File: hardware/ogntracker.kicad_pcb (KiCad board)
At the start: 2 copper layers, 50 x 84 mm, 14 parts, among them J1 ANT, J2 CONN_PWR, U1 STM32DEVBOARD, U2 RFM69HW, U3 VK2828U7G5LF

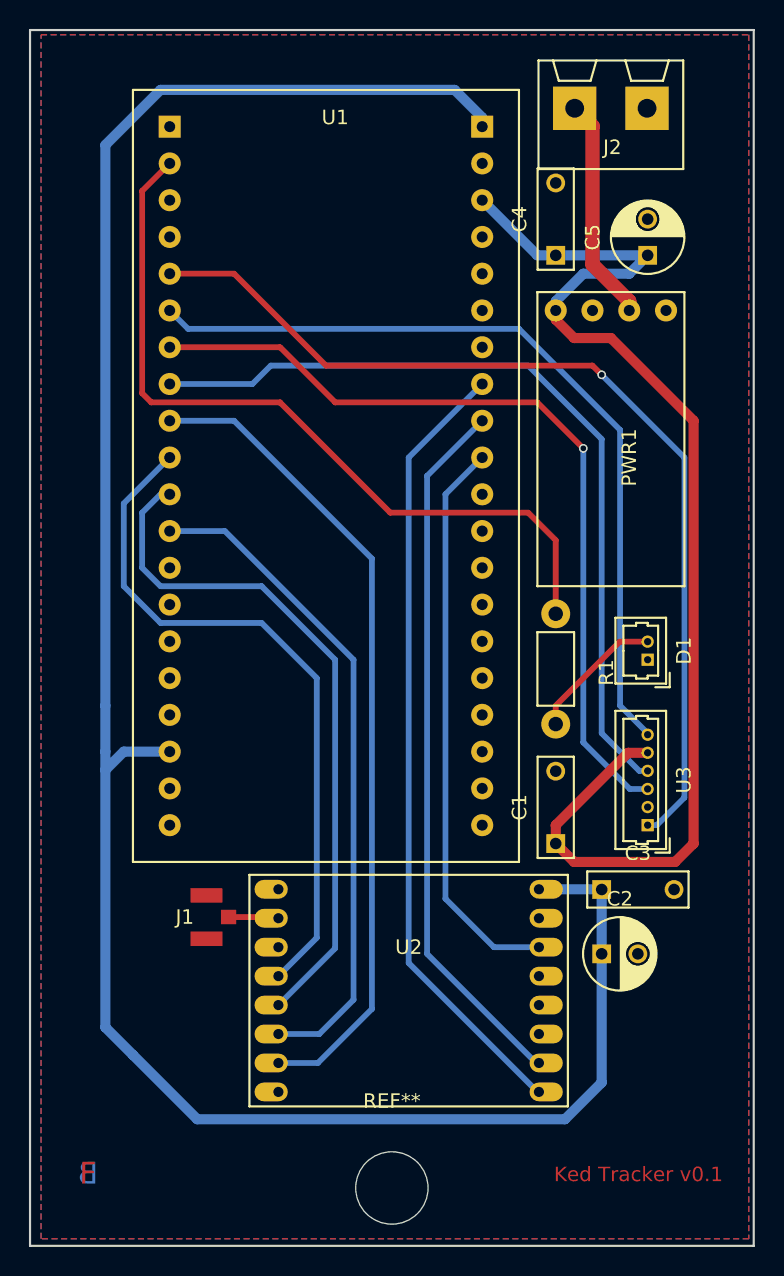
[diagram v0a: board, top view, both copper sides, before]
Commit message: Improvements to make hand-made board easier to produce
 * Wider copper base for pins
 * Proper size of CPU board
 * Added console headers
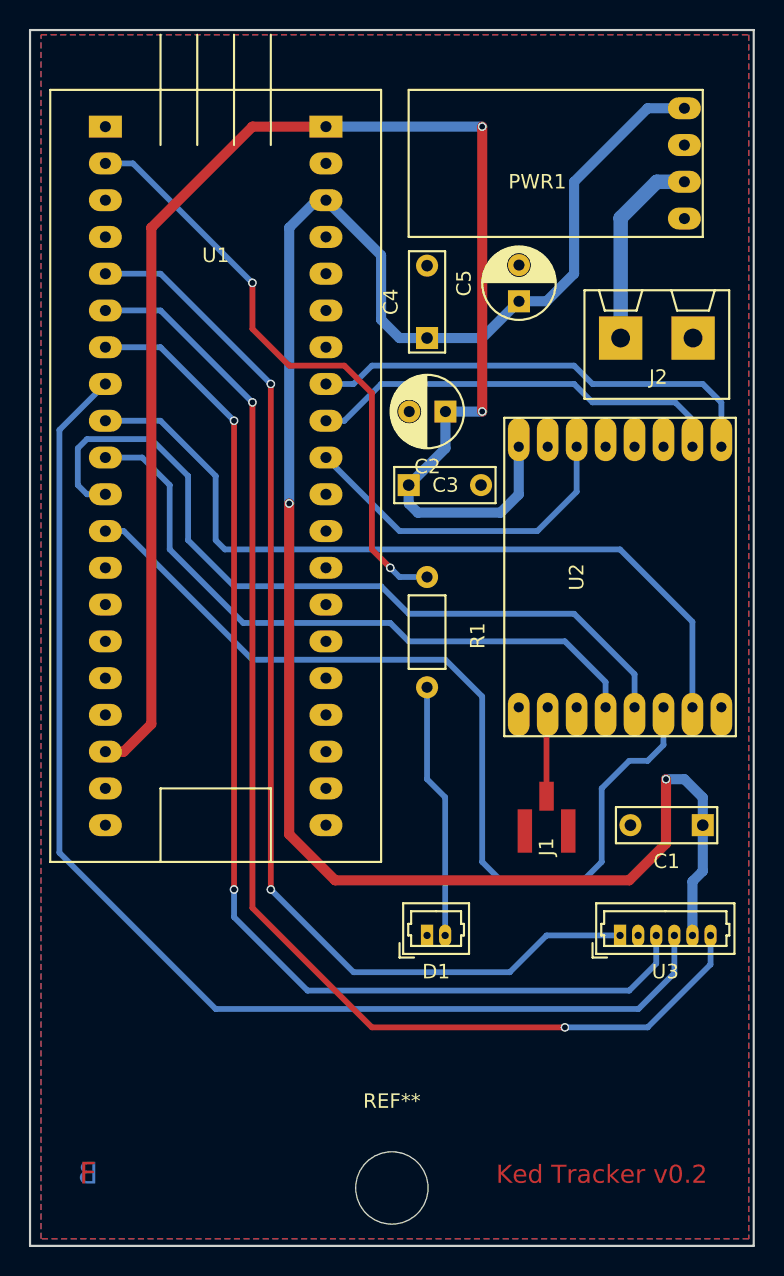
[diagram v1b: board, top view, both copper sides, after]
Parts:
- C1, C3, C4: footprint Capacitors_ThroughHole:C_Rect_L7_W2.5_P5 -> OGN Tracker:C_Rect_L7_W2.5_P5
- C2, C5: footprint Capacitors_ThroughHole:C_Radial_D5_L11_P2.5 -> OGN Tracker:C_Radial_D5_L11_P2.5
- D1: footprint Connectors_Molex:Molex_PicoBlade_53047-0210_02x1.25mm_Straight -> OGN Tracker:Molex_PicoBlade_53047-0210_02x1.25mm_Straight
- J2: footprint Kedder Terminals:XY301-5-2 -> OGN Tracker:XY301-5-2
- R1: footprint Resistors_ThroughHole:Resistor_Horizontal_RM7mm -> OGN Tracker:Resistor_Horizontal_RM7mm
- U3: footprint Connectors_Molex:Molex_PicoBlade_53047-0610_06x1.25mm_Straight -> OGN Tracker:Molex_PicoBlade_53047-0610_06x1.25mm_Straight
- moved C2 39.0 mm to (159.4, 99.1), turned to 180 degrees
- moved U2 32.1 mm to (171.4, 110.5), turned to 270 degrees
- moved C3 31.0 mm to (156.8, 104.1)
- moved D1 24.4 mm to (158.1, 135.3), turned to 0 degrees
- moved J1 24.3 mm to (166.4, 127.6), turned to 90 degrees
- moved J2 16.2 mm to (174.0, 94.0)
- moved PWR1 15.2 mm to (170.8, 81.9), turned to 180 degrees
- moved C4 10.6 mm to (158.1, 94.0)
- moved C1 10.2 mm to (177.2, 127.6), turned to 180 degrees
- moved C5 9.44 mm to (164.5, 91.4)
- moved R1 9.25 mm to (158.1, 110.5)
- moved U1 8.25 mm to (143.5, 102.2)
- moved U3 7.85 mm to (171.4, 135.3), turned to 0 degrees
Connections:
- net Net-(J1-Pad1) renamed /ANT
- net Net-(R1-Pad1) renamed /LED
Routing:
- net 5V: track 83.8 -> 132.6 mm, vias 0 -> 2
- net 3.3V: track 150.6 -> 105.3 mm, vias 0 -> 2
- net /GPS_PPS: track 56.4 -> 86.6 mm, vias 0 -> 2
- net /GPS_RXD: track 57.0 -> 84.3 mm
- net /CHIP_RESET: track 54.8 -> 32.0 mm
- net /GPS_TXD: track 57.6 -> 79.3 mm, vias 1 -> 2
- net /INT_REQ: track 49.3 -> 29.3 mm
- net /SPI_MOSI: track 46.0 -> 64.7 mm
- net /AUX_STATUS: track 39.4 -> 23.7 mm
- net /LED: track 54.5 -> 42.2 mm, vias 0 -> 2
- net /GPS_ENABLE: track 67.6 -> 77.1 mm, vias 1 -> 2
- net Net-(D1-Pad2): track 9.45 -> 17.7 mm
- net /SPI_MISO: track 48.1 -> 55.1 mm
- net /ANT: track 3.50 -> 6.68 mm
- net /SPI_CLOCK: track 47.9 -> 45.3 mm
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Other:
- board text added: "Ked Tracker v0.2"
- board text removed: "Ked Tracker v0.1"

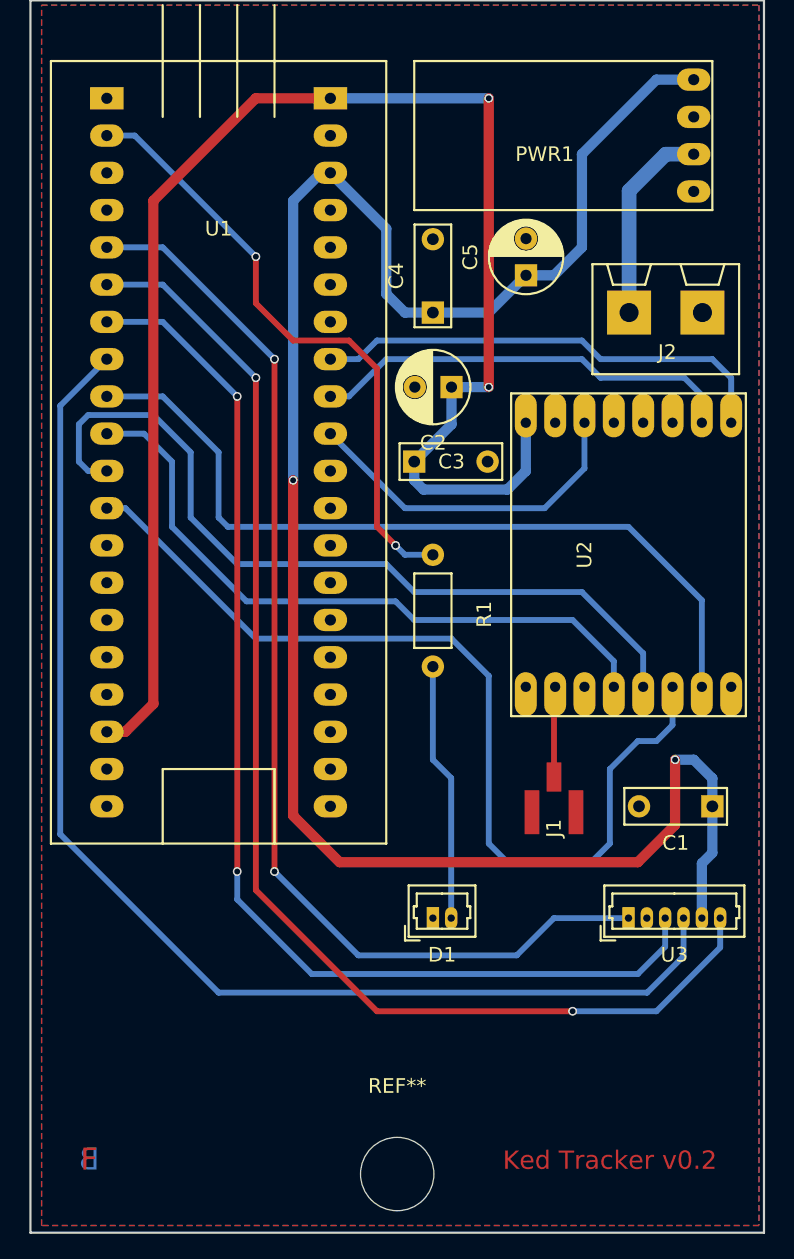
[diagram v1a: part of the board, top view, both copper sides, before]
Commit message: Larger vias and tracks for DIY production
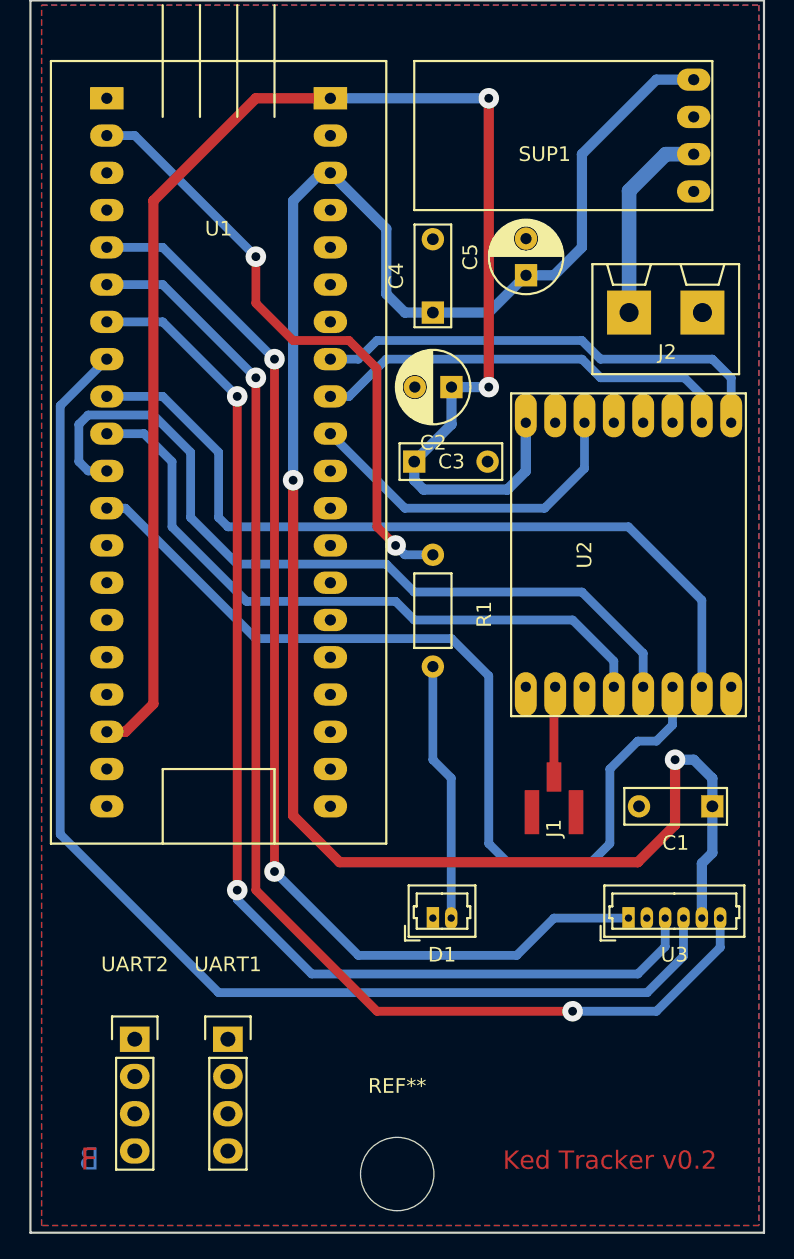
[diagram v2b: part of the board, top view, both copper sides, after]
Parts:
- removed PWR1: BUCK_CONVERTER, OGN Tracker:Buck_Converter_Sm
- added SUP1: BUCK_CONVERTER, OGN Tracker:Buck_Converter_Sm, F.Cu at (170.8, 81.9)
- added UART1: CONSOLE1, Pin_Headers:Pin_Header_Straight_1x04, F.Cu at (144.1, 143.5)
- added UART2: CONSOLE2, Pin_Headers:Pin_Header_Straight_1x04, F.Cu at (137.8, 143.5)
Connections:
- U1 pad 15: (no net) -> /CON2_TXD
- U1 pad 16: (no net) -> /CON2_RXD
- U1 pad 34: (no net) -> /CON1_RXD
- U1 pad 35: (no net) -> /CON1_TXD
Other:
- net class Default: trace_width 0.4 -> 0.6; via_dia 0.6 -> 1.4; via_drill 0.4 -> 0.6
- net class HV: via_dia 0.6 -> 1.4; via_drill 0.4 -> 0.6
- net class PWR: via_dia 0.6 -> 1.4; via_drill 0.4 -> 0.6

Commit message: Version 0.2.0, manufactured
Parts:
- D1: footprint OGN Tracker:Molex_PicoBlade_53047-0210_02x1.25mm_Straight -> Molex_PicoBlade_53047-0210_02x1.25mm_Straight
- U3: footprint OGN Tracker:Molex_PicoBlade_53047-0610_06x1.25mm_Straight -> Molex_PicoBlade_53047-0610_06x1.25mm_Straight
- moved UART1 31.9 mm to (175.9, 146.1)
- moved UART2 30.6 mm to (168.3, 146.1)
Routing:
- net /CON2_TXD: track 0.00 -> 62.7 mm
- net 3.3V: track 105.3 -> 164.8 mm, vias 2 -> 4
- net /CON2_RXD: track 0.00 -> 57.0 mm
- net /CON1_TXD: track 0.00 -> 55.8 mm, vias 0 -> 2
- net /CON1_RXD: track 0.00 -> 55.0 mm, vias 0 -> 2
- net Earth: track 0.00 -> 13.5 mm, vias 0 -> 2
- net /SPI_MOSI: track 64.7 -> 66.9 mm
- net /SPI_SELECT: track 54.8 -> 53.0 mm
- net 5V: track 132.6 -> 134.2 mm
- net /AUX_STATUS: track 23.7 -> 25.1 mm
- net /SPI_MISO: track 55.1 -> 53.7 mm
- net /GPS_RXD: track 84.3 -> 82.9 mm
- net /SPI_CLOCK: track 45.3 -> 44.2 mm
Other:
- net class ANT added: clearance 0.3, trace_width 1, via_dia 1.4, via_drill 0.5
- net class Default: trace_width 0.6 -> 0.5; via_drill 0.6 -> 0.5
- net class HV: via_drill 0.6 -> 0.5
- net class PWR: clearance 0.2 -> 0.3; via_drill 0.6 -> 0.5

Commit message: Hardware 0.3 released for manufacturing
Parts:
- removed UART1: CONSOLE1, Pin_Headers:Pin_Header_Straight_1x04
- removed UART2: CONSOLE2, Pin_Headers:Pin_Header_Straight_1x04
- added BARO1: BMP280, OGN Tracker:BMP280, F.Cu at (175.5, 79.3)
- added C10: 1uF, Capacitors_SMD:C_1206_HandSoldering, F.Cu at (178.5, 119.2)
- added C11: 100nF, Capacitors_SMD:C_1206_HandSoldering, F.Cu at (176.0, 86.2)
- added C6: 1uF, Capacitors_SMD:C_1206_HandSoldering, F.Cu at (178.5, 134.4)
- added C7: 1uF, Capacitors_SMD:C_1206_HandSoldering, F.Cu at (165.8, 133.9)
- added C8: 1uF, Capacitors_SMD:C_1206_HandSoldering, F.Cu at (178.5, 126.8)
- added C9: 1uF, Capacitors_SMD:C_1206_HandSoldering, F.Cu at (172.4, 140.0)
- added D2: 1N4001, Diodes_ThroughHole:Diode_DO-35_SOD27_Horizontal_RM10, F.Cu at (153.1, 141.5)
- added J3: IGC, OGN Tracker:RJ45_SOCKET_SHLD, F.Cu at (141.7, 152.1)
- added L1: 1uH, Inductors:INDUCTOR_V, F.Cu at (157.7, 145.6)
- added R2: 10K, Resistors_SMD:R_1206_HandSoldering, F.Cu at (163.6, 75.5)
- added R3: 10K, Resistors_SMD:R_1206_HandSoldering, F.Cu at (163.6, 78.0)
- added REF***: OSHW-Logo2_7.3x6mm_SilkScreen, Symbols:OSHW-Logo2_7.3x6mm_SilkScreen, B.Cu at (146.0, 126.5)
- added REF***: KiCad-Logo2_6mm_SilkScreen, Symbols:KiCad-Logo2_6mm_SilkScreen, B.Cu at (145.8, 113.8)
- added U4: MAX232, OGN Tracker:DIP-16_W7.62mm, F.Cu at (176.0, 136.2)
- C1, C3: footprint OGN Tracker:C_Rect_L7_W2.5_P5 -> Capacitors_SMD:C_1206_HandSoldering
- C2: footprint OGN Tracker:C_Radial_D5_L11_P2.5 -> Capacitors_SMD:C_1206_HandSoldering
- C4: value 100nF -> 1uF; footprint OGN Tracker:C_Rect_L7_W2.5_P5 -> Capacitors_SMD:C_1206_HandSoldering
- C5: value 10uF -> 330uF; footprint OGN Tracker:C_Radial_D5_L11_P2.5 -> Capacitors_ThroughHole:C_Radial_D8_L13_P3.8
- D1: footprint Molex_PicoBlade_53047-0210_02x1.25mm_Straight -> OGN Tracker:Molex_PicoBlade_53047-0210_02x1.25mm_Straight
- J2: value CONN_PWR -> LX; footprint OGN Tracker:XY301-5-2 -> OGN Tracker:RJ45_SOCKET_SHLD
- R1: value R -> 330; footprint OGN Tracker:Resistor_Horizontal_RM7mm -> Resistors_SMD:R_1206_HandSoldering
- SUP1: value BUCK_CONVERTER -> BUCK_CVTR
- U3: footprint Molex_PicoBlade_53047-0610_06x1.25mm_Straight -> OGN Tracker:Molex_PicoBlade_53047-0610_06x1.25mm_Straight
- moved SUP1 59.9 mm to (145.0, 135.9)
- moved J2 58.2 mm to (169.7, 152.1), turned to 0 degrees
- moved U3 56.8 mm to (133.5, 93.1), turned to 270 degrees
- moved D1 54.5 mm to (133.5, 86.7), turned to 270 degrees
- moved C1 48.4 mm to (134.1, 105.6), turned to 270 degrees
- moved C5 45.6 mm to (157.2, 136.4), turned to 0 degrees
- moved R1 39.0 mm to (134.1, 79.8)
- moved C3 12.0 mm to (161.4, 93.0), turned to 270 degrees
- moved J1 11.3 mm to (163.0, 116.9)
- moved C4 11.2 mm to (163.5, 84.1), turned to 180 degrees
- moved U2 9.62 mm to (171.4, 100.9)
- moved U1 4.57 mm to (148.1, 101.9)
- moved C2 2.55 mm to (161.4, 100.6), turned to 270 degrees
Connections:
- C4 pad 1: 5V -> Earth
- C4 pad 2: Earth -> 5V
- C5 pad 1: 5V -> /SUP_CLEAN
- D1 pad 1: Earth -> 3.3V
- J2 pad 1: Earth -> 5V
- J2 pad 2: +12V -> 5V
- SUP1 pad 2: +12V -> /SUP_CLEAN
- U1 pad 15: /CON2_TXD -> (no net)
- U1 pad 16: /CON2_RXD -> (no net)
- U1 pad 26: (no net) -> /BARO_SDA
- U1 pad 27: (no net) -> /BARO_SCL
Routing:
- net /GPS_RXD: track 82.9 -> 6.98 mm
- net /GPS_TXD: track 79.3 -> 7.52 mm, vias 2 -> 0
- net /GPS_PPS: track 86.6 -> 15.9 mm, vias 2 -> 0
- net /GPS_ENABLE: track 77.1 -> 8.81 mm, vias 2 -> 0
- net /CON2_TXD: track 62.7 -> 0.00 mm
- net /CON2_RXD: track 57.0 -> 0.00 mm
- net /RS232_TX: track 0.00 -> 54.0 mm
- net /RS232_RX: track 0.00 -> 48.8 mm, vias 0 -> 1
- net /BARO_SCL: track 0.00 -> 37.8 mm, vias 0 -> 1
- net /LED: track 42.2 -> 7.93 mm, vias 2 -> 0
- net /BARO_SDA: track 0.00 -> 33.7 mm
- net /SPI_MOSI: track 66.9 -> 39.2 mm, vias 0 -> 1
- net 5V: track 134.2 -> 115.4 mm, vias 2 -> 1
- net /SUP_CLEAN: track 0.00 -> 18.2 mm
- net /CON1_TXD: track 55.8 -> 43.5 mm, vias 2 -> 0
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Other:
- outline, holes or cut-outs redrawn
- net class ANT: via_dia 1.4 -> 0.5; via_drill 0.5 -> 0.3
- net class Default: via_dia 1.4 -> 0.5; via_drill 0.5 -> 0.3
- net class HV: via_dia 1.4 -> 0.5; via_drill 0.5 -> 0.3
- net class PWR: clearance 0.3 -> 0.2; trace_width 0.7 -> 0.5; via_dia 1.4 -> 0.5; via_drill 0.5 -> 0.3
- board text added: "ANTENNA"
- board text added: "Based on design by http://glidernet.org. See https://github.com/kedder/kedtracker for more info."
- board text added: "GPS"
- board text added: "IGC"
- board text added: "Ked Tracker v0.3"
- board text added: "LX"
- board text added: "STATUS LED"
- board text removed: "B"
- board text removed: "F"
- board text removed: "Ked Tracker v0.2"
